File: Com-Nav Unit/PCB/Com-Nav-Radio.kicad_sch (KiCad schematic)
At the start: 102 parts, among them J1 GT-USB-7055, Q10 SS8550, Q11 SS8550, Q12 SS8550, Q13 SS8550, Q14 SS8550, Q15 SS8550, Q16 SS8550, Q2 SS8550, Q3 SS8550, Q4 SS8550, Q5 SS8550, Q6 SS8550, Q7 SS8550, Q8 SS8550, Q9 SS8550, SW1 EC12D1524403, SW10 SW_Push, SW2 EC12E1240301, SW3 EC12D1524403, SW4 EC12E1240301, SW7 SW_Push, SW8 SW_Push, SW9 SW_Push, U1 STM32F411CEUx, U10 FJ2352BH, U11 FJ2352BH, U12 FJ2352BH, U13 FJ2352BH, U14 FJ2352BH, U2 74HC595, U3 74HC595, U4 XC6206P332MR, U5 FJ2352BH, U6 FJ2352BH, U7 FJ2352BH, U8 FJ2352BH, U9 FJ2352BH, Y2 25 MHz

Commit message: PCB - Changed to common cathode with 2 more shift reg
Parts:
- removed C4: 2.2u, symbol Device:C_Small
- removed Q10, Q11, Q12, Q13, Q14, Q15, Q16, Q2, Q3, Q4, Q5, Q6, Q7, Q8, Q9: SS8550, Package_TO_SOT_SMD:SOT-23, symbol Transistor_BJT:SS8550
- removed R25, R26, R27, R28, R29, R30, R31, R32, R33, R34, R35: 100, Resistor_SMD:R_0603_1608Metric, symbol Device:R_Small
- removed R36: 0, Resistor_SMD:R_0603_1608Metric, symbol Device:R_Small
- removed R8: 10k, Resistor_SMD:R_0603_1608Metric, symbol Device:R_Small
- added C14, C17, C18: 2.2u, Capacitor_SMD:C_0603_1608Metric, symbol Device:C_Small
- added C15, C16: 100n, Capacitor_SMD:C_0603_1608Metric, symbol Device:C_Small
- added FB2: GZ2012D601TF, Inductor_SMD:L_0805_2012Metric, symbol Device:FerriteBead_Small
- added J2: TC2030, Connector:Tag-Connect_TC2030-IDC-NL_2x03_P1.27mm_Vertical, symbol Connector:TC2030
- added Q2, Q3, Q4, Q5, Q6, Q7, Q8, Q9: AO3401A, Package_TO_SOT_SMD:SOT-23, symbol Transistor_FET:AO3401A
- added R50, R51, R52, R53, R54, R55, R56, R57: 10k, Resistor_SMD:R_0603_1608Metric, symbol Device:R_Small
- added U15, U16: 74HC595, Package_SO:SOIC-16_3.9x9.9mm_P1.27mm, symbol 74xx:74HC595
- added U17, U18, U19, U20, U21: ULN2003A, Package_SO:SOIC-16_3.9x9.9mm_P1.27mm, symbol Transistor_Array:ULN2003A
- C1, C2: footprint (none) -> Capacitor_SMD:C_0402_1005Metric
- C10, C11, C12, C13, C3, C5, C6, C7, C8, C9: footprint (none) -> Capacitor_SMD:C_0603_1608Metric
- R10, R11, R12, R13, R14, R15, R16, R17, R18, R19, R20, R9: value 10k -> 100; PN 0603WAF1002T5E -> 0603WAF1000T5E
- SW10, SW7, SW8, SW9: footprint (none) -> Button_Switch_THT:SW_PUSH_6mm
- U10, U11, U12, U13, U14, U5, U6, U7, U8, U9: value FJ2352BH -> FJ2352; footprint Custom_7seg:FJ2352BH -> Custom_7seg:FJ2352; symbol Custom_7seg:FJ2352BH -> Custom_7seg:FJ2352; PN FJ2352BH -> FJ2352AH
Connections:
- net SEG2_1 is gone; now on net SEG1: U10.11 (A), U11.11 (A), U12.11 (A), U13.11 (A), U14.11 (A)
- net SEG2_2 is gone; now on net SEG2: U10.7 (B), U11.7 (B), U12.7 (B), U13.7 (B), U14.7 (B)
- net SEG2_3 is gone; now on net SEG3: U10.4 (C), U11.4 (C), U12.4 (C), U13.4 (C), U14.4 (C)
- net SEG2_4 is gone; now on net SEG4: U10.2 (D), U11.2 (D), U12.2 (D), U13.2 (D), U14.2 (D)
- net SEG2_5 is gone; now on net SEG5: U10.1 (E), U11.1 (E), U12.1 (E), U13.1 (E), U14.1 (E)
- net SEG2_6 is gone; now on net SEG6: U10.10 (F), U11.10 (F), U12.10 (F), U13.10 (F), U14.10 (F)
- net SEG2_7 is gone; now on net SEG7: U10.5 (G), U11.5 (G), U12.5 (G), U13.5 (G), U14.5 (G)
- net SEG2_8 is gone; now on net SEG8: U10.3 (DP), U11.3 (DP), U12.3 (DP), U13.3 (DP), U14.3 (DP)
- net +3.3V: now also C8.1, C9.1, U2.16 (VCC), U3.16 (VCC), C15.1, C16.1, U15.16 (VCC), U16.16 (VCC)
- net +5V: now also R6.2, R7.2; no longer C8.1, C9.1, U2.16 (VCC), U3.16 (VCC)
- net DIG1: now also U17.16 (O1); no longer U10.12 (DIG1)
- net DIG10: now also U18.14 (O3); no longer U14.12 (DIG1)
- net DIG11: now also U18.13 (O4); no longer U14.9 (DIG2)
- net DIG12: now also U18.12 (O5); no longer U14.8 (DIG3)
- net DIG13: now also U18.11 (O6); no longer U13.12 (DIG1)
- net DIG14: now also U18.10 (O7); no longer U13.9 (DIG2)
- net DIG15: now also U19.16 (O1); no longer U13.8 (DIG3)
- net DIG2: now also U17.15 (O2); no longer U10.9 (DIG2)
- net DIG3: now also U17.14 (O3); no longer U10.8 (DIG3)
- net DIG4: now also U17.13 (O4); no longer U11.12 (DIG1)
- net DIG5: now also U17.12 (O5); no longer U11.9 (DIG2)
- net DIG6: now also U17.11 (O6); no longer U11.8 (DIG3)
- net DIG7: now also U17.10 (O7); no longer U12.12 (DIG1)
- net DIG8: now also U18.16 (O1); no longer U12.9 (DIG2)
- net DIG9: now also U18.15 (O2); no longer U12.8 (DIG3)
- net ENC1_A: no longer R43.2, SW3.A
- net ENC1_B: no longer R44.2, SW3.B
- net ENC2_A: no longer R45.2, SW4.A
- net ENC2_B: no longer R46.2, SW4.B
- net ENC3_A: now also R43.2, SW3.A
- net ENC3_B: now also R44.2, SW3.B
- net ENC4_A: now also R45.2, SW4.A
- net ENC4_B: now also R46.2, SW4.B
- net GND: now also C14.2, C15.2, C16.2, C17.2, C18.2, U15.8 (GND), U16.8 (GND), U17.8 (GND), U18.8 (GND), U19.8 (GND), U20.8 (GND), U21.3 (I3), U21.4 (I4), U21.5 (I5), U21.6 (I6), U21.7 (I7), U21.8 (GND)
- net at R20.1: now also Q5.3 (D)
- net at R13.2: now also Q5.1 (G), R53.1; no longer U2.7 (QH)
- net at R21.1: now also Q6.3 (D); no longer U1.18 (PB0)
- net at R5.1, U2.11 (SRCLK), U2.12 (RCLK)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: now also U15.12 (RCLK), U16.12 (RCLK)
- net at U1.20 (PB2): now also R37.2; no longer R23.1
- net at R19.1: now also Q4.3 (D)
- net at U3.5 (QF): now also U18.7 (I7); no longer R19.2
- net at R6.1: now also U15.10 (~{SRCLR})
- net at C1.1, U1.6 (PH1): now also Y2.3; no longer Y2.1
- net at U3.3 (QD): now also U18.5 (I5); no longer R17.2
- net at R10.2: now also Q2.1 (G), R50.1; no longer U2.4 (QE)
- net at U2.2 (QC): now also U17.3 (I3)
- net at R16.2: now also Q8.1 (G), R56.1; no longer U3.2 (QC)
- net at R18.1: now also Q3.3 (D)
- net at R11.2: now also Q3.1 (G), R51.1; no longer U2.5 (QF)
- net at C2.1, U1.5 (PH0): now also Y2.1; no longer Y2.3
- net at R22.1: now also Q7.3 (D); no longer U1.19 (PB1)
- net at FB1.1, J1.A4 (VBUS), J1.A9 (VBUS)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: now also FB2.1
- net at R9.1: now also Q2.3 (D)
- net at U2.3 (QD): now also U17.4 (I4); no longer R9.2
- net at U2.15 (QA): now also U17.1 (I1); no longer R6.2
- net at R24.1: now also Q9.3 (D); no longer U1.39 (PB3)
- net at R12.2: now also Q4.1 (G), R52.1; no longer U2.6 (QG)
- net at R4.1, U2.13 (~{OE}), U3.13 (~{OE}): now also U15.13 (~{OE}), U16.13 (~{OE})
- net at R15.2: now also Q7.1 (G), R55.1; no longer U3.1 (QB)
- net at U3.15 (QA): now also U18.2 (I2); no longer R14.2
- net at U3.4 (QE): now also U18.6 (I6); no longer R18.2
- net at U3.6 (QG): now also U19.1 (I1); no longer R20.2
- net at U3.7 (QH): now also U19.2 (I2)
- net at U3.9 (QH'): now also U15.14 (SER)
- net at R7.1: now also U16.10 (~{SRCLR})
- net at U2.1 (QB): now also U17.2 (I2); no longer R7.2
- net SEG1_1 renamed SEG1
- net SEG1: now also R9.2; no longer R21.2
- net SEG1_2 renamed SEG2
- net SEG2: now also R18.2; no longer R22.2
- net SEG1_3 renamed SEG3
- net SEG3: now also R19.2; no longer R23.2, R37.2
- net SEG1_4 renamed SEG4
- net SEG4: now also R20.2; no longer R24.2
- net SEG1_5 renamed SEG5
- net SEG5: now also R21.2
- net SEG1_6 renamed SEG6
- net SEG6: now also R22.2
- net SEG1_7 renamed SEG7
- net SEG7: now also R23.2
- net SEG1_8 renamed SEG8
- net SEG8: now also R24.2
- new net: C14.1, C17.1, C18.1, FB2.2, Q2.2 (S), Q3.2 (S), Q4.2 (S), Q5.2 (S), Q6.2 (S), Q7.2 (S), Q8.2 (S), Q9.2 (S), R50.2, R51.2, R52.2, R53.2, R54.2, R55.2, R56.2, R57.2
- new net: U15.5 (QF), U20.1 (I1)
- new net: U15.6 (QG), U20.2 (I2)
- new net: U15.7 (QH), U20.3 (I3)
- new net: U16.15 (QA), U20.4 (I4)
- new net: U16.1 (QB), U20.5 (I5)
- new net: U16.2 (QC), U20.6 (I6)
- new net: U16.3 (QD), U20.7 (I7)
- new net: U15.9 (QH'), U16.14 (SER)
- new net: U16.4 (QE), U21.1 (I1)
- new net: U16.5 (QF), U21.2 (I2)
- new net: U18.1 (I1), U2.7 (QH)
- new net: U18.3 (I3), U3.1 (QB)
- new net: U18.4 (I4), U3.2 (QC)
- new net: Q9.1 (G), R17.2, R57.1
- new net: Q6.1 (G), R14.2, R54.1
- new net: Q8.3 (D), R23.1
- new net: U15.15 (QA), U19.3 (I3)
- new net: U15.1 (QB), U19.4 (I4)
- new net: U15.2 (QC), U19.5 (I5)
- new net: U15.3 (QD), U19.6 (I6)
- new net: U15.4 (QE), U19.7 (I7)
- new net: U17.5 (I5), U2.4 (QE)
- new net: U17.6 (I6), U2.5 (QF)
- new net: U17.7 (I7), U2.6 (QG)
- new net DIG16: U10.12 (DIG1), U19.15 (O2)
- new net DIG17: U10.9 (DIG2), U19.14 (O3)
- new net DIG18: U10.8 (DIG3), U19.13 (O4)
- new net DIG19: U11.12 (DIG1), U19.12 (O5)
- new net DIG20: U11.9 (DIG2), U19.11 (O6)
- new net DIG21: U11.8 (DIG3), U19.10 (O7)
- new net DIG22: U12.12 (DIG1), U20.16 (O1)
- new net DIG23: U12.9 (DIG2), U20.15 (O2)
- new net DIG24: U12.8 (DIG3), U20.14 (O3)
- new net DIG25: U14.12 (DIG1), U20.13 (O4)
- new net DIG26: U14.9 (DIG2), U20.12 (O5)
- new net DIG27: U14.8 (DIG3), U20.11 (O6)
- new net DIG28: U13.12 (DIG1), U20.10 (O7)
- new net DIG29: U13.9 (DIG2), U21.16 (O1)
- new net DIG30: U13.8 (DIG3), U21.15 (O2)
- new net SWO: U1.39 (PB3)
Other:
- note removed: "R36 allows driving DP together between the 2 segment bus. Allows DMA control of the segments"
- moved on the sheet: C10, C11, C12, C13, C5, C6, C7, C8, C9, FB1, R1, R2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

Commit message: PCB - Add swd connector, add switches
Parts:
- removed J2: TC2030, Connector:Tag-Connect_TC2030-IDC-NL_2x03_P1.27mm_Vertical, symbol Connector:TC2030
- added D1, D2, D3, D4, D5, D6: SM4007PL, Diode_SMD:D_SOD-123F, symbol Device:D_Small
- added F1: MF-NSMF050-2, Fuse:Fuse_1206_3216Metric, symbol Device:Polyfuse
- added J2: Conn_02x05_Odd_Even, Connector_PinHeader_1.27mm:PinHeader_2x05_P1.27mm_Vertical_SMD, symbol Connector_Generic:Conn_02x05_Odd_Even
- added J3: Conn_01x04_Pin, Connector_PinHeader_2.54mm:PinHeader_1x04_P2.54mm_Vertical, symbol Connector:Conn_01x04_Pin
- added Q10: AO3401A, Package_TO_SOT_SMD:SOT-23, symbol Transistor_FET:AO3401A
- added R25: 100, Resistor_SMD:R_0603_1608Metric, symbol Device:R_Small
- added R58, R8: 10k, Resistor_SMD:R_0603_1608Metric, symbol Device:R_Small
- added RV1, RV2: R_Potentiometer, symbol Device:R_Potentiometer
- added U22: USBLC6-2SC6, Package_TO_SOT_SMD:SOT-23-6, symbol Power_Protection:USBLC6-2SC6
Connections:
- net +3.3V: now also R1.2, R2.2, R6.2, R7.2, Q10.2 (S), R8.2, RV1.1, RV2.1
- net BOOT0: now also SW9.2, D4.1 (K)
- net DIG1: now also D1.2 (A)
- net DIG2: now also D2.2 (A)
- net DIG3: now also D3.2 (A)
- net DIG4: now also D4.2 (A)
- net DIG5: now also D5.2 (A)
- net DIG6: now also D6.2 (A)
- net ENC2_A: now also U1.29 (PA8); no longer U1.12 (PA2)
- net ENC2_B: now also U1.30 (PA9); no longer U1.13 (PA3)
- net ENC3_A: now also U1.40 (PB4); no longer U1.14 (PA4)
- net ENC3_B: now also U1.17 (PA7); no longer U1.29 (PA8)
- net ENC4_A: now also U1.42 (PB6); no longer U1.30 (PA9)
- net ENC4_B: now also U1.43 (PB7); no longer U1.31 (PA10)
- net GND: now also J2.3 (Pin_3), J2.5 (Pin_5), J2.9 (Pin_9), J3.1 (Pin_1), R58.1, RV1.3, RV2.3, U22.2 (GND)
- net NRST: now also J2.10 (Pin_10)
- net SWDCLK: now also J2.4 (Pin_4), J3.2 (Pin_2)
- net SWDIO: now also J2.2 (Pin_2), J3.3 (Pin_3)
- net SWO: now also J2.6 (Pin_6)
- net USB_D+: no longer J1.A7 (D-), J1.B7 (D-)
- net USB_D-: no longer J1.A6 (D+), J1.B6 (D+)
- net SW_COM: now reaches SW7.1
- net SW_COM: now also SW1.S2, SW10.1, SW3.S2, SW8.1, SW9.1, U1.18 (PB0)
- net at SW7.2: now also D2.1 (K), Q10.3 (D)
- net SEG_CT3: now reaches R12.1
- net SEG_CT3: now also U1.46 (PB9)
- net at SW3.S1: now also D1.1 (K)
- net at R5.2: now also U1.15 (PA5); no longer U1.17 (PA7)
- net SEG_CT7: now reaches R16.1
- net SEG_CT7: now also U1.27 (PB14)
- net SEG_CT4: now reaches R13.1
- net SEG_CT4: now also U1.21 (PB10)
- net at SW8.2: now also D3.1 (K)
- net at J1.A4 (VBUS), J1.A9 (VBUS), J1.B4 (VBUS)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: now also F1.1; no longer FB1.1, FB2.1
- net at R4.1, U15.13 (~{OE}), U16.13 (~{OE})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: now also R8.1
- net at SW10.2: now also D5.1 (K)
- net SEG_CT5: now reaches R14.1
- net SEG_CT5: now also U1.25 (PB12)
- net SEG_CT2: now reaches R11.1
- net SEG_CT2: now also U1.45 (PB8)
- net at SW1.S1: now also D6.1 (K)
- net at R3.2: now also U1.12 (PA2); no longer U1.15 (PA5)
- net at R4.2: now also U1.13 (PA3); no longer U1.16 (PA6)
- net at U1.2 (PC13): now also R25.1
- net SEG_CT6: now reaches U1.26 (PB13)
- net SEG_CT6: now also R15.1
- net SEG_CT8: now reaches U1.28 (PB15)
- net SEG_CT8: now also R17.1
- net SEG_CT1: now reaches U1.41 (PB5)
- net SEG_CT1: now also R10.1
- net +5V: no longer names the net of C5.1, C6.1, FB1.2, U4.3 (VI)
- net +5V: no longer R1.2, R2.2, R6.2, R7.2
- new net: F1.2, FB1.1, FB2.1, U22.5 (VBUS)
- new net: J1.A6 (D+), J1.B6 (D+), U22.3 (I/O2)
- new net: J1.A7 (D-), J1.B7 (D-), U22.1 (I/O1)
- new net +3V3: J2.1 (Pin_1), J3.4 (Pin_4)
- new net BOOT0_DIS: Q10.1 (G), R25.2, R58.2
- new net POT1: RV1.2, U1.14 (PA4)
- new net POT2: RV2.2, U1.16 (PA6)
- new net USB_DN: U22.4 (I/O2)
- new net USB_DP: U22.6 (I/O1)
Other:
- moved on the sheet: C15, C16, C8, C9, Q2, Q3, Q4, Q5, Q6, Q7, Q8, Q9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

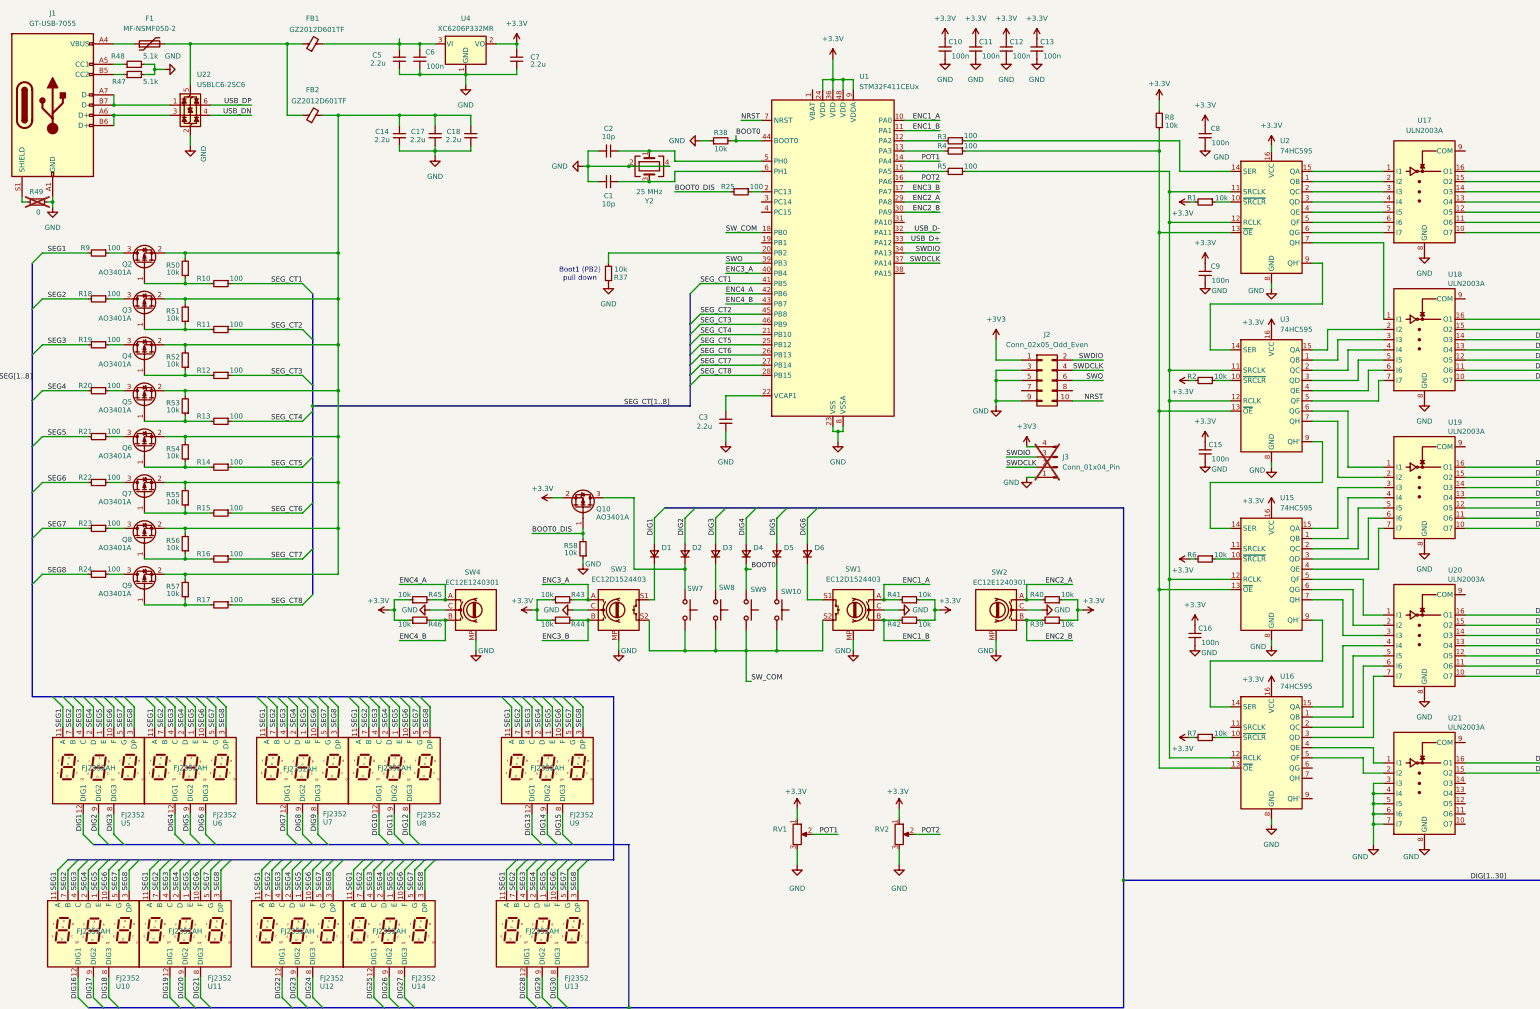
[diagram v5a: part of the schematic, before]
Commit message: PCB - SCH - first drc run, add no connect flags
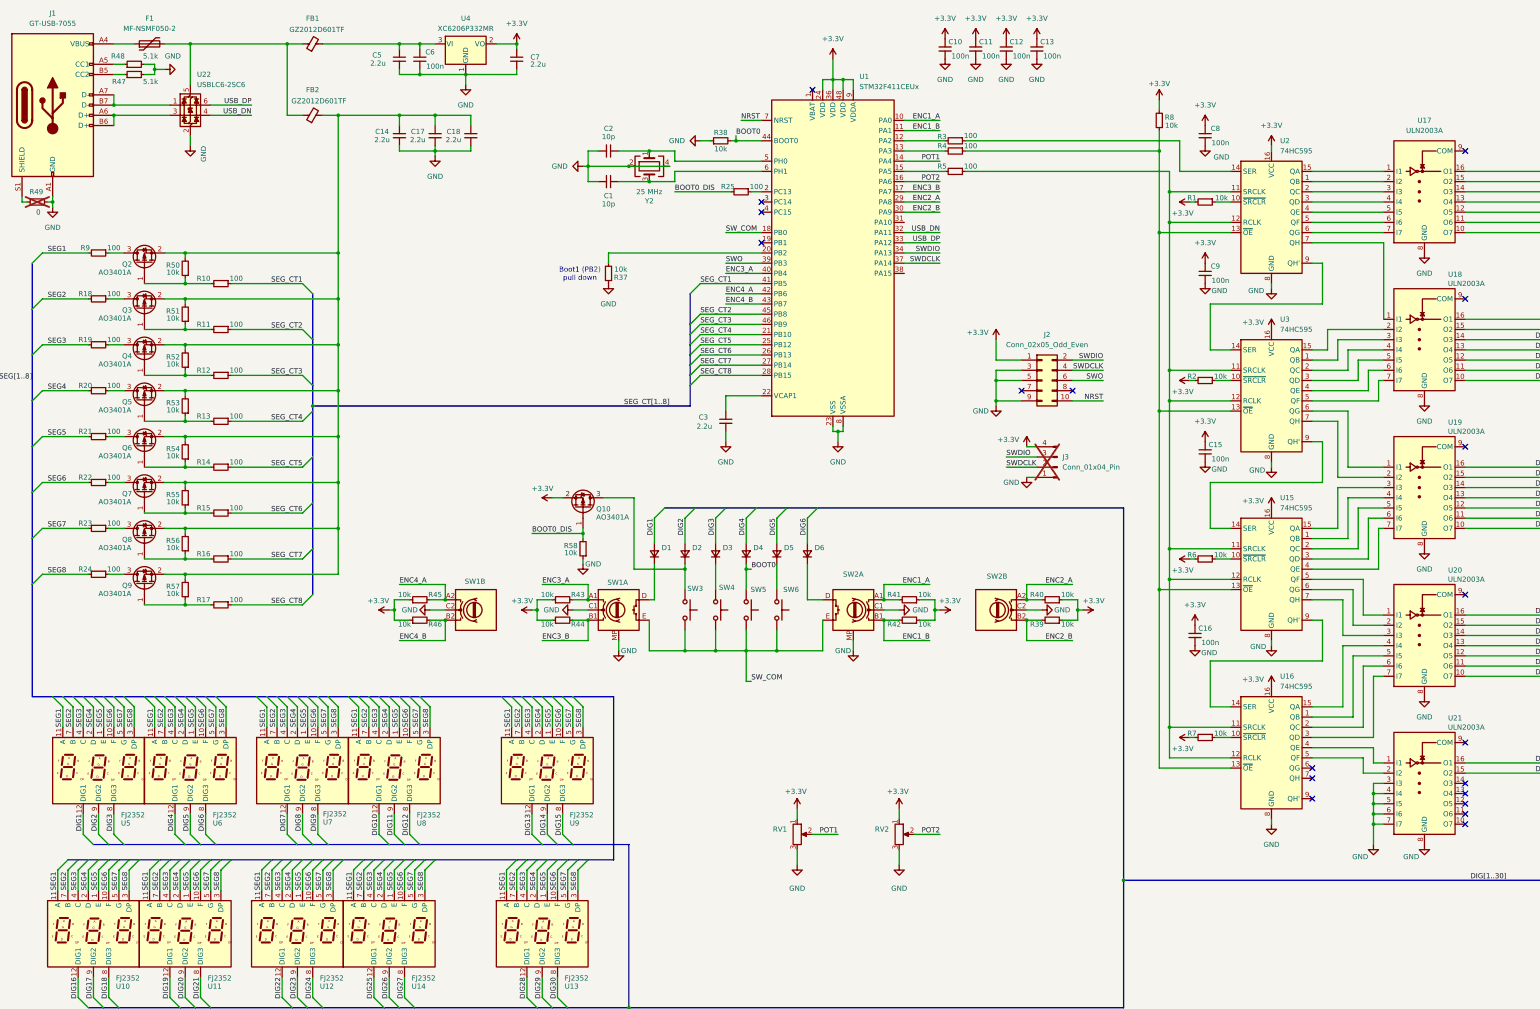
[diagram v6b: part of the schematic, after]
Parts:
- removed SW1, SW3: EC12D1524403, Encoder:EC12D1524403, symbol Device:RotaryEncoder_Switch_MP
- removed SW2, SW4: EC12E1240301, Encoder:EC12E1240301, symbol Encoders:RotaryEncoder_MP
- added SW1, SW2: ~, symbol Encoders:Dual_Encoder_Push
- renumbered SW7 to SW3, SW8 to SW4, SW9 to SW5, SW10 to SW6
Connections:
- net +3V3 is gone; now on net +3.3V: J2.1 (Pin_1), J3.4 (Pin_4)
- net USB_D+ is gone; now on net USB_DP: U1.33 (PA12)
- net USB_D- is gone; now on net USB_DN: U1.32 (PA11)
- net ENC1_A: now also SW2.A1
- net ENC1_B: now also SW2.B1
- net ENC2_A: now also SW2.A2
- net ENC2_B: now also SW2.B2
- net ENC3_A: now also SW1.A1
- net ENC3_B: now also SW1.B1
- net ENC4_A: now also SW1.A2
- net ENC4_B: now also SW1.B2
- net GND: now also SW1.C1, SW1.C2, SW1.MP, SW2.C1, SW2.C2, SW2.MP
- net SW_COM: now also SW1.E, SW2.E
- net at D1.1 (K): now also SW1.D
- net at R5.1, U15.12 (RCLK), U16.12 (RCLK)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: now also U15.11 (SRCLK), U16.11 (SRCLK)
- net at D6.1 (K): now also SW2.D
- no-connect marks 0 -> 19
